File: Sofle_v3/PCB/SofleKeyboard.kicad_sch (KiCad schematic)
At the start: 103 parts, among them J1 LED, J2 4PIN, J3 OLED, J4 key leds, J5 backlight sel, J6 indicator bypass, P1 i2c_pin, P2 i2c_pin, SW1 SW_PUSH-MX_W_LED, SW10 SW_PUSH-MX_W_LED, SW11 SW_PUSH-MX_W_LED, SW12 SW_PUSH-MX_W_LED, SW13 SW_PUSH-MX_W_LED, SW14 SW_PUSH-MX_W_LED, SW15 SW_PUSH-MX_W_LED, SW16 SW_PUSH-MX_W_LED, SW17 SW_PUSH-MX_W_LED, SW18 SW_PUSH-MX_W_LED, SW19 SW_PUSH-MX_W_LED, SW2 SW_PUSH-MX_W_LED, SW20 SW_PUSH-MX_W_LED, SW21 SW_PUSH-MX_W_LED, SW22 SW_PUSH-MX_W_LED, SW23 SW_PUSH-MX_W_LED, SW24 SW_PUSH-MX_W_LED, SW25 Rotary_Encoder_Switch, SW26 SW_PUSH-MX_W_LED, SW27 SW_PUSH-MX_W_LED, SW28 SW_PUSH-MX_W_LED, SW29 SW_PUSH-MX_W_LED, SW3 SW_PUSH-MX_W_LED, SW30 SW_PUSH-MX_W_LED, SW4 SW_PUSH-MX_W_LED, SW5 SW_PUSH-MX_W_LED, SW6 SW_PUSH-MX_W_LED, SW7 SW_PUSH-MX_W_LED, SW8 SW_PUSH-MX_W_LED, SW9 SW_PUSH-MX_W_LED, U1 ProMicro

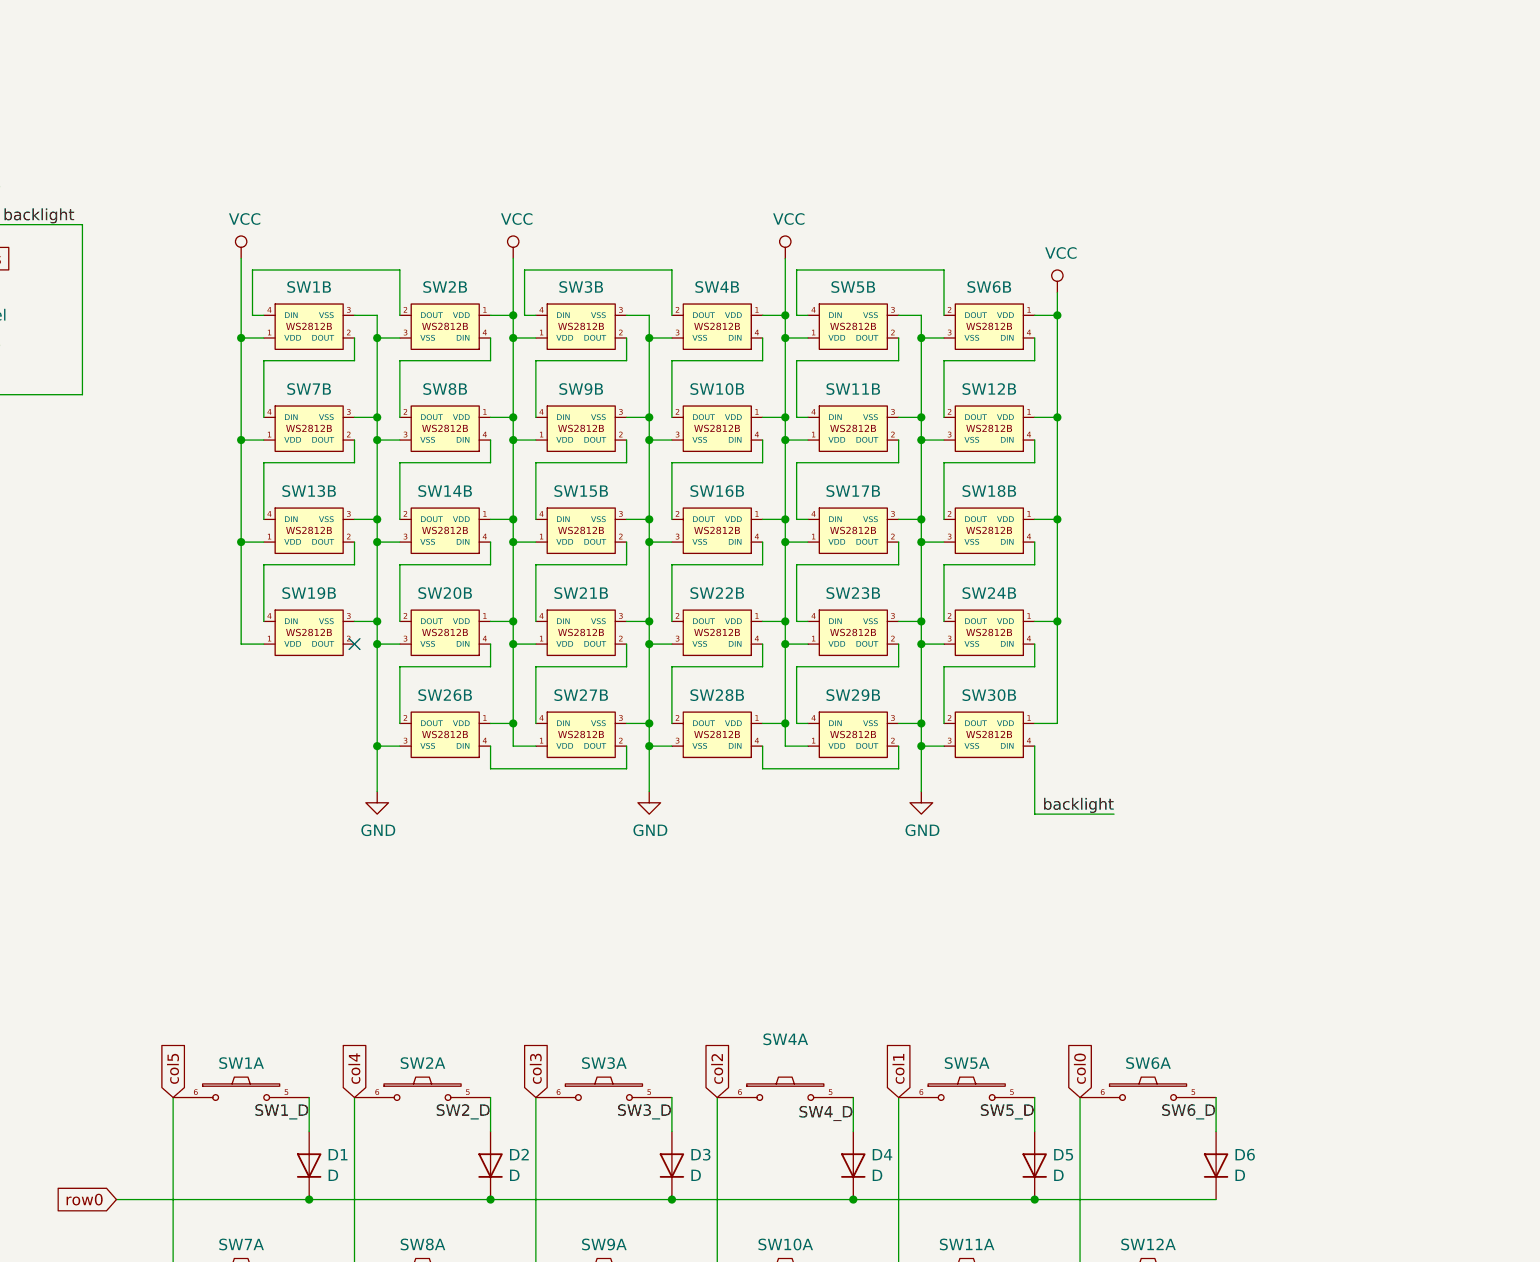
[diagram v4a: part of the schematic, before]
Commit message: design: removed cutout for daughter board + increased led distance
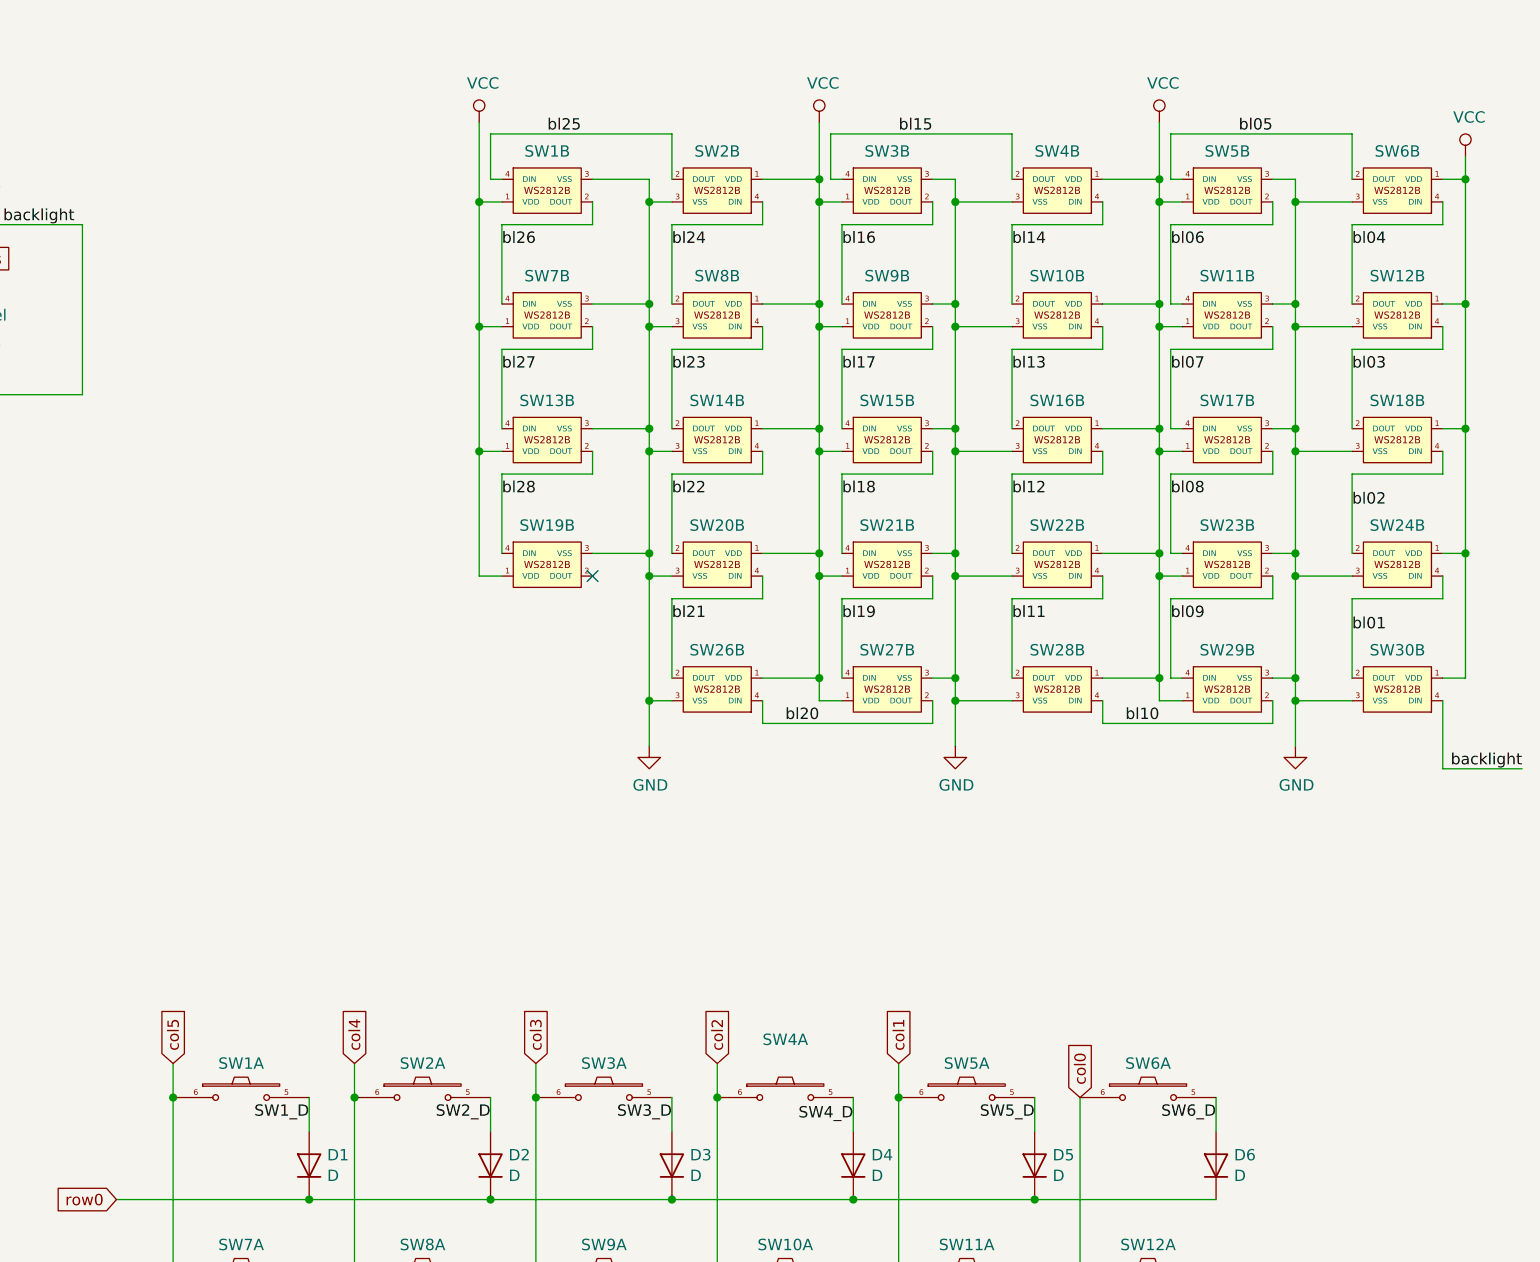
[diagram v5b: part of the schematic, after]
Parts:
- SW25: footprint SofleRGB:EVQWGD001_DaughterBoard -> (none)
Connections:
- net bl26: now reaches SW1.2 (DOUT), SW7.4 (DIN)
- net bl25: now reaches SW1.4 (DIN), SW2.2 (DOUT)
- net bl24: now reaches SW2.4 (DIN), SW8.2 (DOUT)
- net bl16: now reaches SW3.2 (DOUT), SW9.4 (DIN)
- net bl15: now reaches SW3.4 (DIN), SW4.2 (DOUT)
- net bl14: now reaches SW10.2 (DOUT), SW4.4 (DIN)
- net bl06: now reaches SW11.4 (DIN), SW5.2 (DOUT)
- net bl05: now reaches SW5.4 (DIN), SW6.2 (DOUT)
- net bl04: now reaches SW12.2 (DOUT), SW6.4 (DIN)
- net bl27: now reaches SW13.4 (DIN), SW7.2 (DOUT)
- net bl23: now reaches SW14.2 (DOUT), SW8.4 (DIN)
- net bl17: now reaches SW15.4 (DIN), SW9.2 (DOUT)
- net bl13: now reaches SW10.4 (DIN), SW16.2 (DOUT)
- net bl07: now reaches SW11.2 (DOUT), SW17.4 (DIN)
- net bl03: now reaches SW12.4 (DIN), SW18.2 (DOUT)
- net bl02: now reaches SW18.4 (DIN), SW24.2 (DOUT)
- net bl01: now reaches SW24.4 (DIN), SW30.2 (DOUT)
- net bl09: now reaches SW23.2 (DOUT), SW29.4 (DIN)
- net bl08: now reaches SW17.2 (DOUT), SW23.4 (DIN)
- net bl12: now reaches SW16.4 (DIN), SW22.2 (DOUT)
- net bl11: now reaches SW22.4 (DIN), SW28.2 (DOUT)
- net bl19: now reaches SW21.2 (DOUT), SW27.4 (DIN)
- net bl18: now reaches SW15.2 (DOUT), SW21.4 (DIN)
- net bl22: now reaches SW14.4 (DIN), SW20.2 (DOUT)
- net bl21: now reaches SW20.4 (DIN), SW26.2 (DOUT)
- net bl28: now reaches SW13.2 (DOUT), SW19.4 (DIN)
- net bl10: now reaches SW28.4 (DIN), SW29.2 (DOUT)
- net bl20: now reaches SW26.4 (DIN), SW27.2 (DOUT)
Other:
- moved on the sheet: SW10B, SW11B, SW12B, SW13B, SW14B, SW15B, SW16B, SW17B, SW18B, SW19B, SW1B, SW20B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

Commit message: design: Daughter board - Redesign and added pcb project - Some 3d model shenanigans
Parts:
- D1, D10, D11, D12, D13, D14, D15, D16, D17, D18, D19, D2, D20, D21, D22, D23, D24, D25, D26, D27, D28, D29, D3, D30, D4, D5, D6, D7, D8, D9: footprint Diode_SMD:crkbd-diode -> SofleRGB:crkbd-diode
- SW25: footprint (none) -> SofleRGB:EVQWGD001_DaughterBoard_only

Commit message: design: daughter board update
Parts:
- removed JP10, JP11, JP12, JP13, JP14, JP9: Jumper_3_Open_Custom, SofleRGB:CustomJumper, symbol SofleKeyboard:Jumper_3_Open_Custom
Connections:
- net RES_A is gone; now on net ENCA: SW25.A
- net RES_B is gone; now on net GND: SW25.B
- net RES_C is gone; now on net ENCB: SW25.C
- net RES_S1 is gone; now on net col5: SW25.S1
- net RES_S2 is gone; now on net SW25B: SW25.S2
- net RES_D: no longer names the net of SW25.D
- no-connect marks 6 -> 5

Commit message: design: replaced staggered uC design with solder jumpers
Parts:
- removed U1: ProMicro, SofleKeyboard-footprint:ProMicro, symbol SofleKeyboard-rescue:ProMicro_2-Lily58-cache-Lily58_Pro-rescue
- added JP011, JP012, JP021, JP022, JP031, JP032, JP041, JP042, JP051, JP052, JP061, JP062, JP071, JP072, JP081, JP082, JP091, JP092, JP101, JP102, JP111, JP112, JP121, JP122, JP131, JP132, JP141, JP142, JP151, JP152, JP161, JP162, JP171, JP172, JP181, JP182, JP191, JP192, JP201, JP202, JP211, JP212, JP221, JP222, JP231, JP232, JP241, JP242: Jumper_2_Open, SofleRGB:CustomSolderJumper, symbol Jumper:Jumper_2_Open
- added U100: ProMicroDualSided, SofleRGB:ProMicroSingle, symbol SofleKeyboard:ProMicroDualSided
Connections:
- net DATA: now also JP021.2 (B), JP232.2 (B)
- net ENCA: now also JP052.2 (B), JP201.2 (B)
- net ENCB: now also JP062.2 (B), JP191.2 (B)
- net GND: now also JP022.2 (B), JP031.2 (B), JP041.2 (B), JP212.2 (B), JP222.2 (B), JP231.2 (B)
- net LED: now also JP011.2 (B), JP242.2 (B)
- net RESET: now also JP032.2 (B), JP221.2 (B)
- net SCL: now also JP061.2 (B), JP192.2 (B)
- net SDA: now also JP051.2 (B), JP202.2 (B)
- net VCC: now also JP042.2 (B), JP211.2 (B)
- net col0: now also JP072.2 (B), JP181.2 (B)
- net col1: now also JP082.2 (B), JP171.2 (B)
- net col2: now also JP092.2 (B), JP161.2 (B)
- net col3: now also JP102.2 (B), JP151.2 (B)
- net col4: now also JP112.2 (B), JP141.2 (B)
- net col5: now also JP122.2 (B), JP131.2 (B)
- net row0: now also JP081.2 (B), JP172.2 (B)
- net row1: now also JP091.2 (B), JP162.2 (B)
- net row2: now also JP101.2 (B), JP152.2 (B)
- net row3: now also JP111.2 (B), JP142.2 (B)
- net row4: now also JP121.2 (B), JP132.2 (B)
- new net A00|D05: JP171.1 (A), JP172.1 (A), U100.17 (D05|A00)
- new net A01|D04: JP181.1 (A), JP182.1 (A), U100.18 (D04|A01)
- new net A02|SCL: JP191.1 (A), JP192.1 (A), U100.19 (SCL|A02)
- new net A03|SDA: JP201.1 (A), JP202.1 (A), U100.20 (SDA|A03)
- new net D04|A01: JP071.1 (A), JP072.1 (A), U100.7 (D04|A1)
- new net D05|A00: JP081.1 (A), JP082.1 (A), U100.8 (D05|A0)
- new net D06|D15: JP091.1 (A), JP092.1 (A), U100.9 (D06|D15)
- new net D07|D14: JP101.1 (A), JP102.1 (A), U100.10 (D07|D14)
- new net D08|D16: JP111.1 (A), JP112.1 (A), U100.11 (D08|D16)
- new net D09|D10: JP121.1 (A), JP122.1 (A), U100.12 (D09|D10)
- new net D10|D09: JP131.1 (A), JP132.1 (A), U100.13 (D09|D10)
- new net D14|D07: JP151.1 (A), JP152.1 (A), U100.15 (D07|D14)
- new net D15|D06: JP161.1 (A), JP162.1 (A), U100.16 (D06|D15)
- new net D16|D08: JP141.1 (A), JP142.1 (A), U100.14 (D08|D16)
- new net GND|RST: JP031.1 (A), JP032.1 (A), U100.3 (GND|RST)
- new net GND|RXD: JP231.1 (A), JP232.1 (A), U100.23 (RXD|GND)
- new net GND|VCC: JP041.1 (A), JP042.1 (A), U100.4 (GND|VCC)
- new net RAW|TXD: JP241.1 (A), JP242.1 (A), U100.24 (TXD|RAW)
- new net RST|GND: JP221.1 (A), JP222.1 (A), U100.22 (GND|RST)
- new net RXD|GND: JP021.1 (A), JP022.1 (A), U100.2 (RXD|GND)
- new net SCL|A02: JP061.1 (A), JP062.1 (A), U100.6 (SCL|A2)
- new net SDA|A03: JP051.1 (A), JP052.1 (A), U100.5 (SDA|A3)
- new net TXD|RAW: JP011.1 (A), JP012.1 (A), U100.1 (TXD|RAW)
- new net VCC|GND: JP211.1 (A), JP212.1 (A), U100.21 (GND|VCC)
- no-connect marks 5 -> 7
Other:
- moved on the sheet: D1, D10, D11, D12, D13, D14, D15, D16, D17, D18, D19, D2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
